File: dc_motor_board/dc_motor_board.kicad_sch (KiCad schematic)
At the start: 55 parts, among them J1 Prog (PinHeader_2x03_P2.54mm), J2 DG142R-5.08-04P-14 IN24V, J5 DebugUSART (PinHeader_01x03_P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, J6 Debug GPIO (PinHeader_01x02_P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, Q1 DTC114ECA (SOT-23), Q2 DTC114ECA (SOT-23), Q3 IRF4905SPbF (D2PAK), U1 ADM3485EARZ-REEL (SOIC-8), U2 PAI141M30 (SOIC-16), U3 STM32G070RBTx (LQFP-64)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

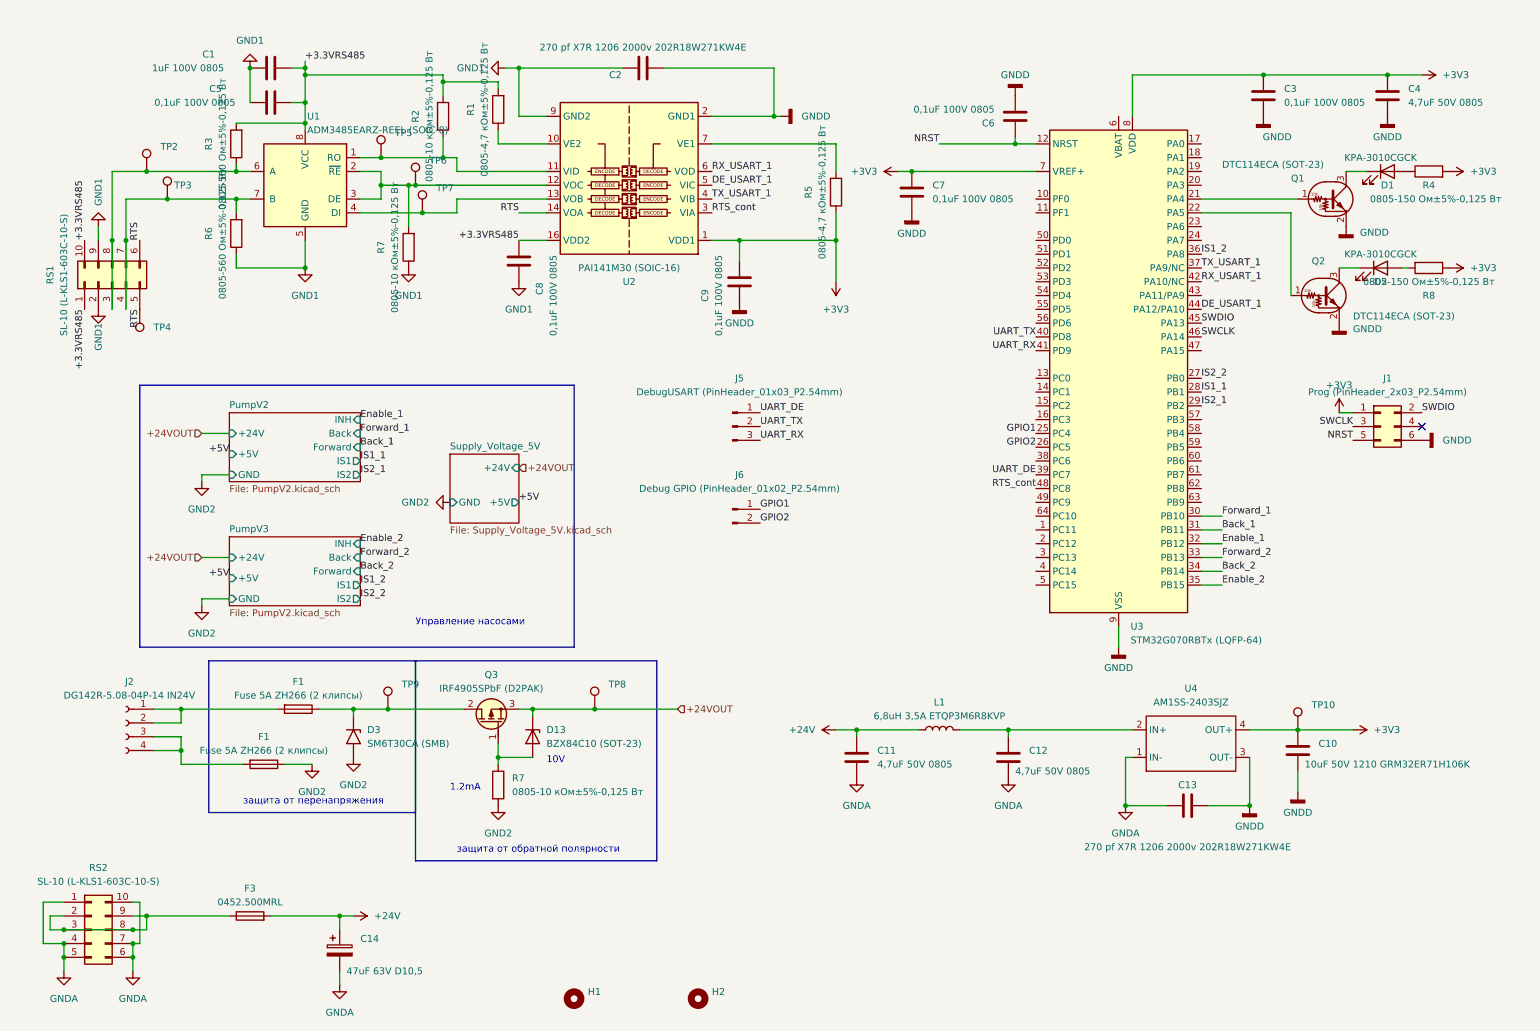
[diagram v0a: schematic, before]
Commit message: fix dc board issues before manufacturing
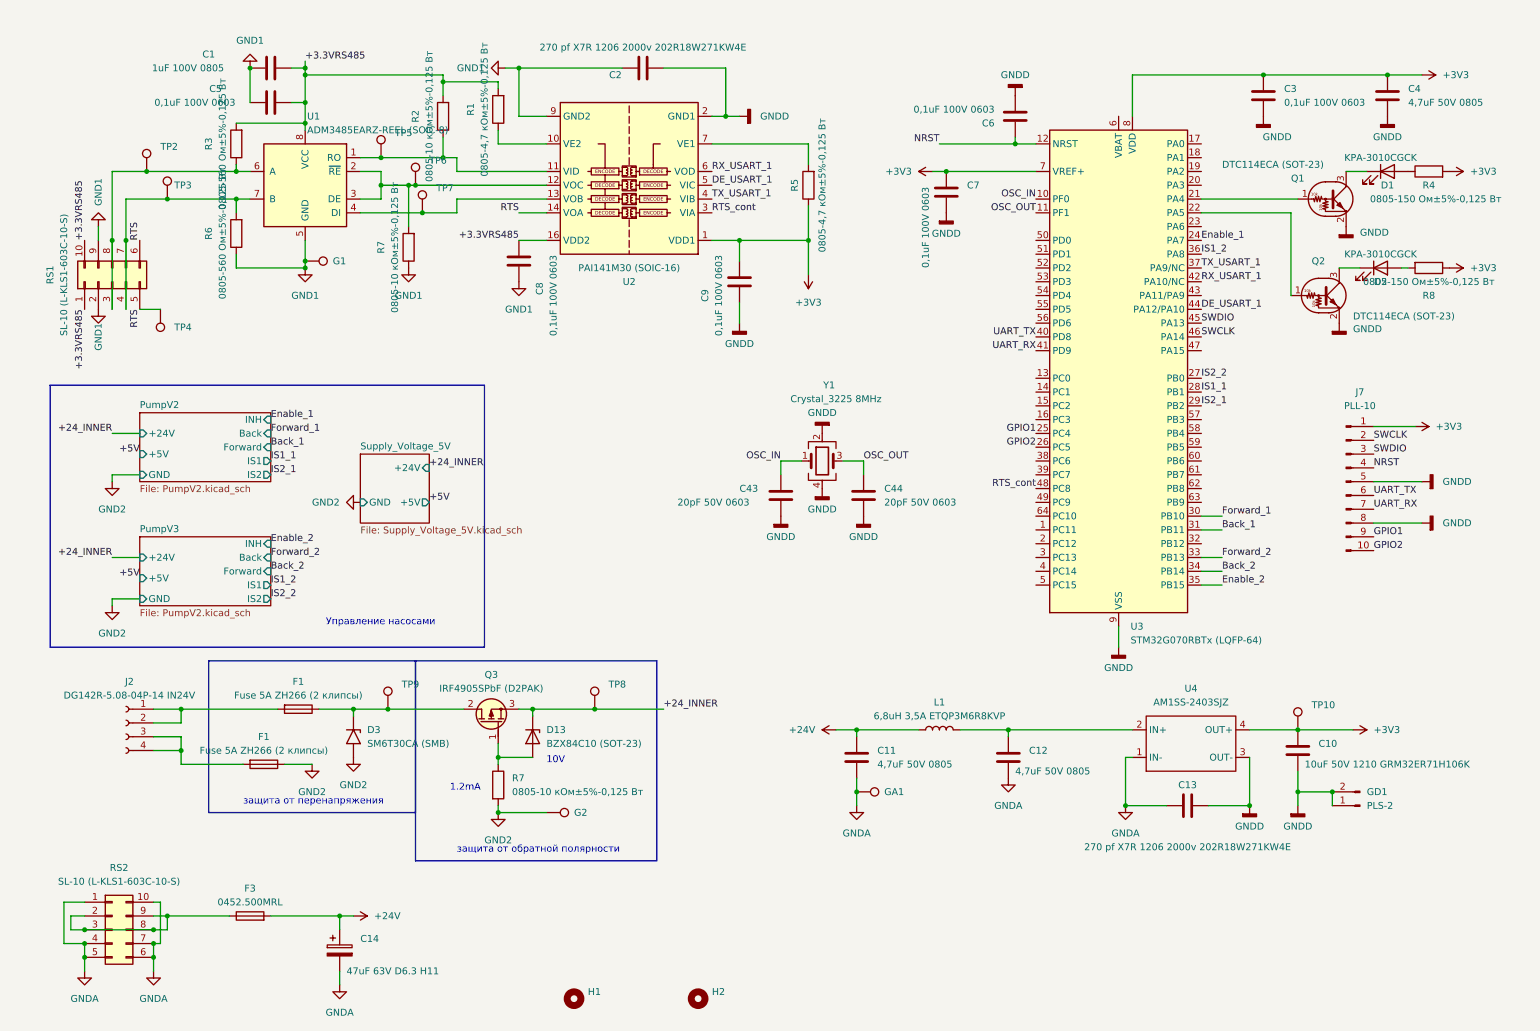
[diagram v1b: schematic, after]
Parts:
- removed J1: Prog (PinHeader_2x03_P2.54mm), Connector_PinHeader_2.54mm:PinHeader_2x03_P2.54mm_Vertical, symbol Connector_Generic:Conn_02x03_Odd_Even
- removed J5: DebugUSART (PinHeader_01x03_P2.54mm), Connector_PinHeader_2.54mm:PinHeader_1x03_P2.54mm_Vertical, symbol Connector:Conn_01x03_Pin
- removed J6: Debug GPIO (PinHeader_01x02_P2.54mm), Connector_PinHeader_2.54mm:PinHeader_1x02_P2.54mm_Vertical, symbol Connector:Conn_01x02_Pin
- added C43, C44: 20pF 50V 0603, Capacitor_SMD:C_0603_1608Metric, symbol Device:C
- added G1, G2, GA1: TestPoint, PCM_4ms_TestPoint:TestPoint_D1, symbol Connector:TestPoint
- added GD1: PLS-2, Connector_PinHeader_2.54mm:PinHeader_1x02_P2.54mm_Vertical, symbol Connector:Conn_01x02_Pin
- added J7: PLL-10, Connector_PinHeader_1.27mm:PinHeader_1x10_P1.27mm_Vertical, symbol Connector:Conn_01x10_Pin
- added Y1: Crystal_3225 8MHz, PCM_Crystal_AKL:Crystal_SMD_3225-4Pin_3.2x2.5mm, symbol Device:Crystal_GND24
- C14: value 47uF 63V D10,5 -> 47uF 63V D6.3 H11
- C3, C5, C6, C7, C8, C9: value 0,1uF 100V 0805 -> 0,1uF 100V 0603; footprint PCM_Capacitor_SMD_AKL:C_0805_2012Metric_Pad1.15x1.40mm -> Capacitor_SMD:C_0603_1608Metric_Pad1.08x0.95mm_HandSolder
- J2: value DG142R-5.08-04P-14 IN24V -> DG142R-5.08-04P-14 IN24V
- RS1: now left out of the parts list
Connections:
- net +3V3: now also J7.1 (Pin_1)
- net Enable_1: now also U3.24 (PA7); no longer U3.32 (PB12)
- net GND1: now also G1.1
- net GND2: now also G2.1
- net GNDA: now also GA1.1
- net GNDD: now also C43.2, C44.2, GD1.1 (Pin_1), GD1.2 (Pin_2), J7.5 (Pin_5), J7.8 (Pin_8), Y1.2, Y1.4
- net GPIO1: now also J7.9 (Pin_9)
- net GPIO2: now also J7.10 (Pin_10)
- net NRST: now also J7.4 (Pin_4)
- net SWCLK: now also J7.2 (Pin_2)
- net SWDIO: now also J7.3 (Pin_3)
- net UART_RX: now also J7.7 (Pin_7)
- net UART_TX: now also J7.6 (Pin_6)
- net OSC_IN: now reaches U3.10 (PF0)
- net OSC_IN: now also C43.1, Y1.1
- net OSC_OUT: now reaches U3.11 (PF1)
- net OSC_OUT: now also C44.1, Y1.3
- net +24VOUT renamed +24_INNER
- net UART_DE: no longer names the net of U3.39 (PC7)
- no-connect marks 1 -> 0
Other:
- moved on the sheet: C7, R5, RS2, TP4

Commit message: DC, contr, mb, step v2
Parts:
- GD1: now left out of the parts list
- J7: value PLL-10 -> PLL-10 (Prog)
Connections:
- net GNDD: now also J7.6 (Pin_6); no longer J7.5 (Pin_5), J7.8 (Pin_8)
- net NRST: now also J7.5 (Pin_5); no longer J7.4 (Pin_4)
- net SWCLK: now also J7.3 (Pin_3); no longer J7.2 (Pin_2)
- net SWDIO: now also J7.4 (Pin_4); no longer J7.3 (Pin_3)
- net UART_RX: now also J7.8 (Pin_8); no longer J7.7 (Pin_7)
- net UART_TX: now also J7.7 (Pin_7); no longer J7.6 (Pin_6)
- no-connect marks 0 -> 1
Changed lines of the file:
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@@
   (junction (at 77.47 40.64) (diameter 0) (color 0 0 0 0)
   )
+  (no_connect (at 260.35 87.63))
   (wire (pts (xy 237.49 146.05) (xy 237.49 154.94))
     (stroke (width 0) (type default))
@@
     (stroke (width 0) (type default))
   )
-  (wire (pts (xy 260.35 95.25) (xy 269.24 95.25))
-    (stroke (width 0) (type default))
-  )
   (wire (pts (xy 102.87 45.72) (xy 107.95 45.72))
     (stroke (width 0) (type default))
@@
     (stroke (width 0) (type default))
   )
+  (wire (pts (xy 260.35 97.79) (xy 269.24 97.79))
+    (stroke (width 0) (type default))
+  )
   (wire (pts (xy 63.5 29.21) (xy 63.5 30.48))
     (stroke (width 0) (type default))
@@
     (stroke (width 0) (type default))
   )
-  (wire (pts (xy 260.35 102.87) (xy 269.24 102.87))
-    (stroke (width 0) (type default))
-  )
   (wire (pts (xy 166.37 91.44) (xy 166.37 93.98))
     (stroke (width 0) (type default))
@@
     (effects (font (size 1.27 1.27)) (justify left bottom))
   )
-  (label "UART_RX" (at 260.35 100.33 0) (fields_autoplaced)
+  (label "UART_RX" (at 260.35 102.87 0) (fields_autoplaced)
     (effects (font (size 1.27 1.27)) (justify left bottom))
   )
@@
     (effects (font (size 1.27 1.27)) (justify right bottom))
   )
-  (label "UART_TX" (at 260.35 97.79 0) (fields_autoplaced)
+  (label "UART_TX" (at 260.35 100.33 0) (fields_autoplaced)
     (effects (font (size 1.27 1.27)) (justify left bottom))
   )
@@
     (effects (font (size 1.27 1.27)) (justify left bottom))
   )
-  (label "NRST" (at 260.35 92.71 0) (fields_autoplaced)
+  (label "NRST" (at 260.35 95.25 0) (fields_autoplaced)
     (effects (font (size 1.27 1.27)) (justify left bottom))
   )
@@
     (effects (font (size 1.27 1.27)) (justify left bottom))
   )
-  (label "SWCLK" (at 260.35 87.63 0) (fields_autoplaced)
+  (label "SWCLK" (at 260.35 90.17 0) (fields_autoplaced)
     (effects (font (size 1.27 1.27)) (justify left bottom))
   )
@@
     (effects (font (size 1.27 1.27)) (justify left bottom))
   )
-  (label "SWDIO" (at 260.35 90.17 0) (fields_autoplaced)
+  (label "SWDIO" (at 260.35 92.71 0) (fields_autoplaced)
     (effects (font (size 1.27 1.27)) (justify left bottom))
   )
@@
   )
   (symbol (lib_id "Connector:Conn_01x02_Pin") (at 257.81 154.94 180) (unit 1)
-    (in_bom yes) (on_board yes) (dnp no) (fields_autoplaced)
+    (in_bom no) (on_board yes) (dnp no) (fields_autoplaced)
     (property "Reference" "GD1" (at 259.08 152.4 0)
       (effects (font (size 1.27 1.27)) (justify right))
@@
     )
   )
-  (symbol (lib_id "power:GNDD") (at 269.24 102.87 90) (unit 1)
-    (in_bom yes) (on_board yes) (dnp no) (fields_autoplaced)
-    (property "Reference" "#PWR055" (at 275.59 102.87 0)
-      (effects (font (size 1.27 1.27)) hide)
-    )
-    (property "Value" "GNDD" (at 273.05 102.87 90)
-      (effects (font (size 1.27 1.27)) (justify right))
-    )
-    (property "Footprint" "" (at 269.24 102.87 0)
-      (effects (font (size 1.27 1.27)) hide)
-    )
-    (property "Datasheet" "" (at 269.24 102.87 0)
-      (effects (font (size 1.27 1.27)) hide)
-    )
-    (pin "1")
-    (instances
-      (project "Плата насосов"
-        (path "/7f8f7dc9-8c50-44ed-985c-35a6d8c67be0"
-          (reference "#PWR055") (unit 1)
-        )
-      )
-    )
-  )
   (symbol (lib_id "Connector:TestPoint") (at 83.82 40.64 0) (unit 1)
     (in_bom no) (on_board yes) (dnp no) (fields_autoplaced)
@@
     )
   )
-  (symbol (lib_id "power:GNDD") (at 269.24 95.25 90) (unit 1)
+  (symbol (lib_id "power:GNDD") (at 269.24 97.79 90) (unit 1)
     (in_bom yes) (on_board yes) (dnp no) (fields_autoplaced)
-    (property "Reference" "#PWR056" (at 275.59 95.25 0)
+    (property "Reference" "#PWR056" (at 275.59 97.79 0)
       (effects (font (size 1.27 1.27)) hide)
     )
-    (property "Value" "GNDD" (at 273.05 95.25 90)
+    (property "Value" "GNDD" (at 273.05 97.79 90)
       (effects (font (size 1.27 1.27)) (justify right))
     )
-    (property "Footprint" "" (at 269.24 95.25 0)
+    (property "Footprint" "" (at 269.24 97.79 0)
       (effects (font (size 1.27 1.27)) hide)
     )
-    (property "Datasheet" "" (at 269.24 95.25 0)
+    (property "Datasheet" "" (at 269.24 97.79 0)
       (effects (font (size 1.27 1.27)) hide)
     )
@@
       (effects (font (size 1.27 1.27)))
     )
-    (property "Value" "PLL-10" (at 257.81 81.28 0)
+    (property "Value" "PLL-10 (Prog)" (at 257.81 81.28 0)
       (effects (font (size 1.27 1.27)))
     )

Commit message: DC, contr, mb, digit in v2.1
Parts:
- C3, C5, C6, C7, C8, C9: footprint Capacitor_SMD:C_0603_1608Metric_Pad1.08x0.95mm_HandSolder -> Capacitor_SMD:C_0603_1608Metric

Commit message: controller  убраны ловушки
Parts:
- C1: footprint PCM_Capacitor_SMD_AKL:C_0805_2012Metric_Pad1.18x1.45mm_HandSolder -> Capacitor_SMD:C_0805_2012Metric
- C10: footprint PCM_Capacitor_SMD_AKL:C_1210_3225Metric_Pad1.42x2.65mm_HandSolder -> Capacitor_SMD:C_1210_3225Metric
- C11, C12, C4: footprint PCM_Capacitor_SMD_AKL:C_0805_2012Metric_Pad1.15x1.40mm -> Capacitor_SMD:C_0805_2012Metric
- C13, C2: footprint PCM_Capacitor_SMD_Handsoldering_AKL:C_1210_3225Metric_Pad1.42x2.65mm -> Capacitor_SMD:C_1210_3225Metric
- C14: footprint PCM_Capacitor_THT_AKL:CP_Radial_D6.3mm_P2.50mm -> Capacitor_THT:CP_Radial_D6.3mm_P2.50mm
- F3: footprint PCM_Fuse_Handsoldering_AKL:Fuse_Littelfuse-NANO2-451_453 -> Fuse:Fuse_Littelfuse-NANO2-451_453
- G1, G2, GA1, TP10, TP2, TP3, TP4, TP5, TP6, TP7, TP8, TP9: footprint PCM_4ms_TestPoint:TestPoint_D1 -> TestPoint:TestPoint_Pad_D1.0mm
- GD1, RS2: now in the parts list
- J2: value DG142R-5.08-04P-14 IN24V -> DG142R-5.08-04P-14 IN24V
- L1: footprint PCM_Inductor_SMD_Handsoldering_AKL:L_Bourns-SRN6028 -> Inductor_SMD:L_Bourns-SRN6028
- Q3: footprint PCM_Package_TO_SOT_SMD_AKL:TO-263-2 -> Package_TO_SOT_SMD:TO-263-2; symbol PCM_Transistor_MOSFET_AKL:IRF4905 -> Transistor_FET:IRF4905
- R1, R2, R3, R4, R5, R6, R7, R8: footprint PCM_4ms_Resistor:R_0805_2012Metric -> Resistor_SMD:R_0805_2012Metric
- U2: symbol Isolator:π141M3x -> Isolator 7:π141M3x
- U4: symbol Converter_DCDC:AM1SS- -> Converter_DCDC7:AM1SS-
- Y1: footprint PCM_Crystal_AKL:Crystal_SMD_3225-4Pin_3.2x2.5mm -> Crystal:Crystal_SMD_3225-4Pin_3.2x2.5mm
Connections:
- no-connect marks 1 -> 37
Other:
- moved on the sheet: G1, R3, R7

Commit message: dc Pai capasitor
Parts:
- Y1: footprint Crystal:Crystal_SMD_3225-4Pin_3.2x2.5mm -> Crystal:Crystal_SMD_TXC_7M-4Pin_3.2x2.5mm
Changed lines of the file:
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@@
 			)
 		)
-		(property "Footprint" "Crystal:Crystal_SMD_3225-4Pin_3.2x2.5mm"
+		(property "Footprint" "Crystal:Crystal_SMD_TXC_7M-4Pin_3.2x2.5mm"
 			(at 158.75 91.44 0)
 			(effects

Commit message: all замменил резисторы failsafe в плате контроллера и обрал из перечня во всех остальных
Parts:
- R3, R6: now left out of the parts list
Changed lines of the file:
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@@
 		(unit 1)
 		(exclude_from_sim no)
-		(in_bom yes)
+		(in_bom no)
 		(on_board yes)
 		(dnp no)
@@
 		(unit 1)
 		(exclude_from_sim no)
-		(in_bom yes)
-		(on_board yes)
-		(dnp no)
+		(in_bom no)
+		(on_board yes)
+		(dnp no)

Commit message: step,mother,digitin,dc,controller электронные сборочные
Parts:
- GD1: now left out of the parts list
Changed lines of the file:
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@@
 		(unit 1)
 		(exclude_from_sim no)
-		(in_bom yes)
+		(in_bom no)
 		(on_board yes)
 		(dnp no)

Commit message: update schemas
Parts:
- F3: value 0452.500MRL -> 0451.500MRL
- RS2: now left out of the parts list
- renumbered D13 to D4, F1 to F2, R7 to R9
